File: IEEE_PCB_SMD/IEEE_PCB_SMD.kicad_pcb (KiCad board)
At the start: 2 copper layers, 98.9 x 105.3 mm, 19 parts, among them U1 555, U2 4017, U3 EG1218, U5 CR2025TR

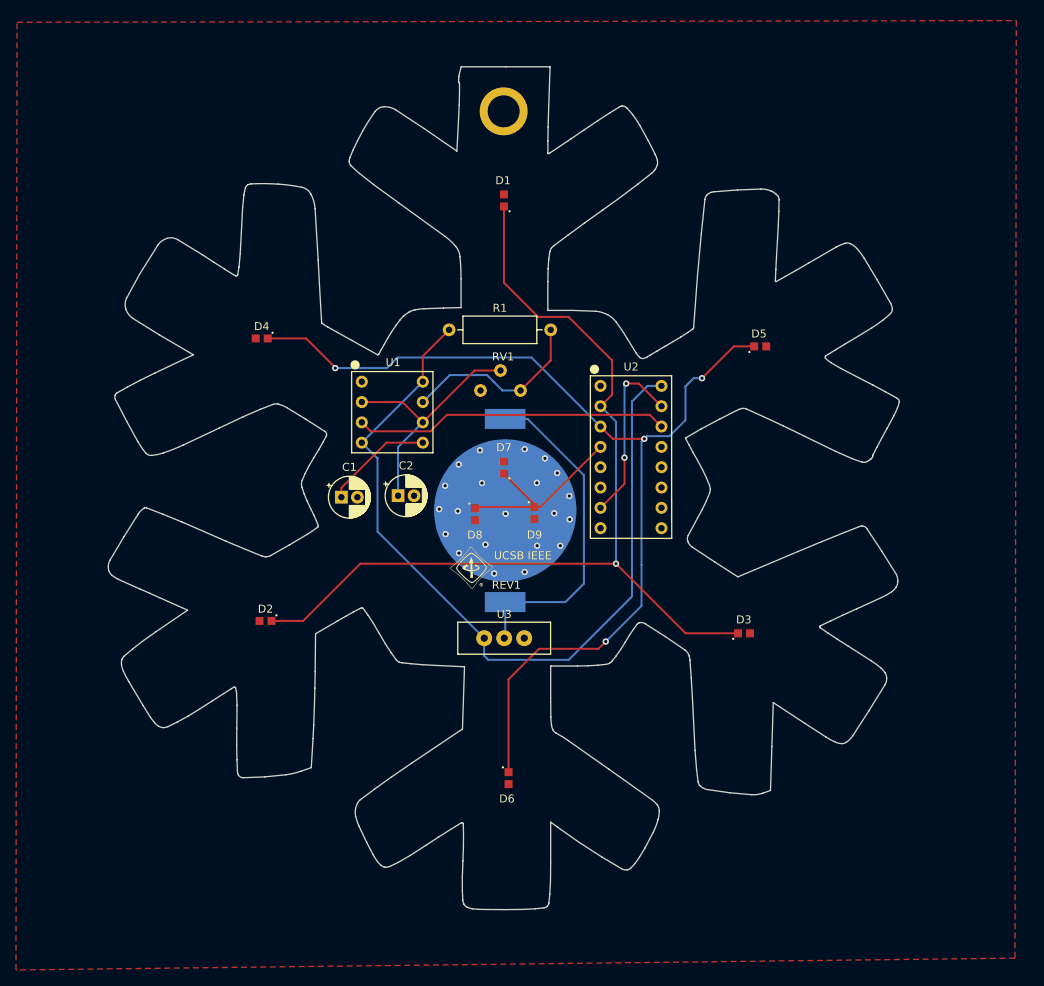
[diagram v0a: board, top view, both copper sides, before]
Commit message: Rev 10/8/22
changed the logo footprint
changed the resistor footprint
added more vias to the power
altered traces to better fit the ESR standards
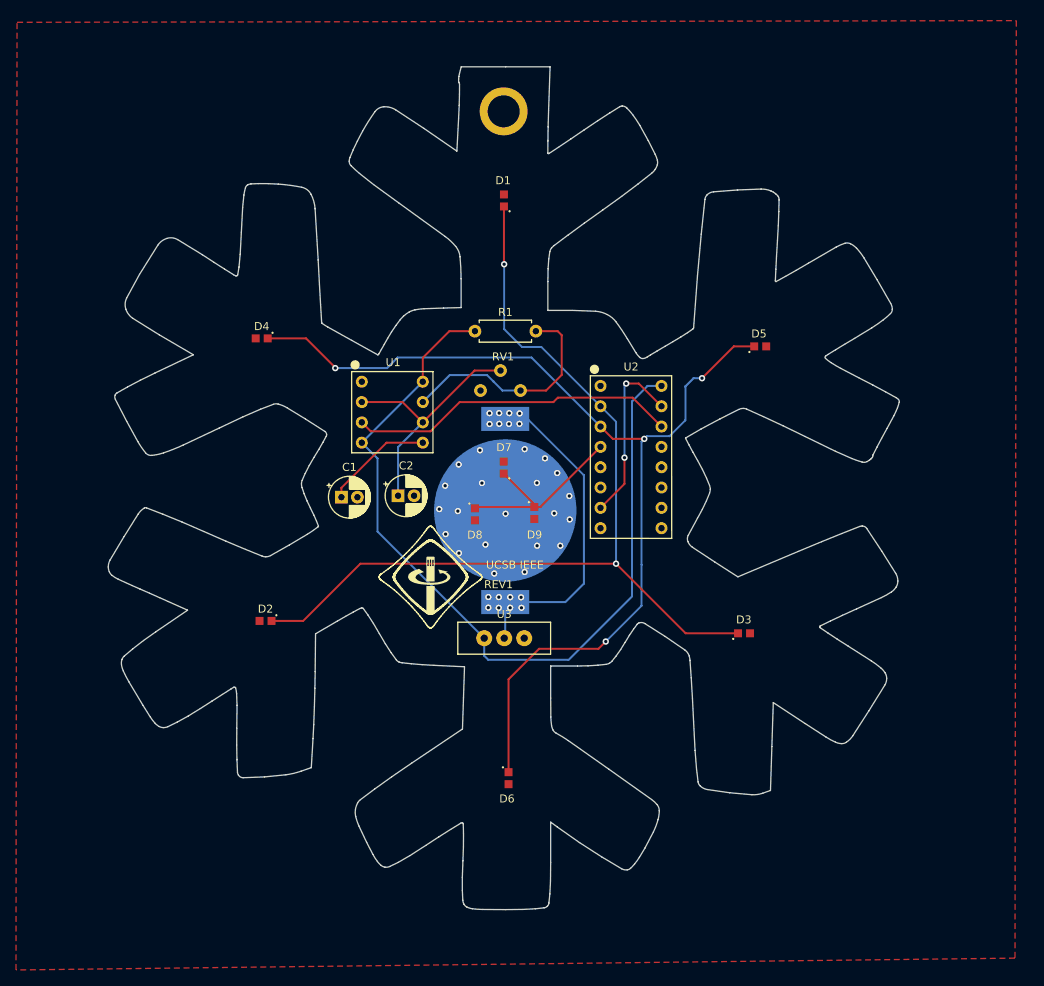
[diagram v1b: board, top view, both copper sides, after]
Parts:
- removed G***: LOGO, custom parts:IEEE Logo
- added REF**: UCSB_IEEE_Logo, custom parts:UCSB_IEEE_Logo, F.Cu at (138.8, 104.1)
- R1: footprint Resistor_THT:R_Axial_DIN0309_L9.0mm_D3.2mm_P12.70mm_Horizontal -> Resistor_THT:R_Axial_DIN0207_L6.3mm_D2.5mm_P7.62mm_Horizontal
- moved R1 3.23 mm to (144.4, 73.3)
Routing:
- net Net-(R1-Pad2): track 23.6 -> 28.8 mm
- net +3V3: track 102.4 -> 105.5 mm
- net Net-(D1-Pad2): track 118.8 -> 116.7 mm, vias 1 -> 2
- net Signal: track 39.4 -> 41.2 mm
- net Net-(U3-Pad2): vias 0 -> 16

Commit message: Rev - Matthew
Snowflake changes:
Fixed battery and switch symbols
added 100 ohm resistors 603
looked at traces - not acid traps that I see

will work on the ball soon
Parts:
- removed U3: EG1218, IEEE_Ornament:EG1218
- removed U5: CR2025TR, IEEE_Ornament:CR2025TR
- added BT1: Battery_Cell, IEEE_Ornament:CR2025TR, F.Cu at (149.5, 95.2)
- added R10: 100, Resistor_SMD:R_0603_1608Metric_Pad0.98x0.95mm_HandSolder, F.Cu at (152.4, 96.0)
- added R2: 100, Resistor_SMD:R_0603_1608Metric_Pad0.98x0.95mm_HandSolder, F.Cu at (149.5, 60.7)
- added R3: 100, Resistor_SMD:R_0603_1608Metric_Pad0.98x0.95mm_HandSolder, F.Cu at (125.9, 105.5)
- added R4: 100, Resistor_SMD:R_0603_1608Metric_Pad0.98x0.95mm_HandSolder, F.Cu at (174.6, 109.8)
- added R5: 100, Resistor_SMD:R_0603_1608Metric_Pad0.98x0.95mm_HandSolder, F.Cu at (124.2, 75.8)
- added R6: 100, Resistor_SMD:R_0603_1608Metric_Pad0.98x0.95mm_HandSolder, F.Cu at (177.7, 76.0)
- added R7: 100, Resistor_SMD:R_0603_1608Metric_Pad0.98x0.95mm_HandSolder, F.Cu at (150.0, 122.4)
- added R8: 100, Resistor_SMD:R_0603_1608Metric_Pad0.98x0.95mm_HandSolder, F.Cu at (149.5, 92.2)
- added R9: 100, Resistor_SMD:R_0603_1608Metric_Pad0.98x0.95mm_HandSolder, F.Cu at (146.8, 96.0)
- added SW1: EG1218, IEEE_Ornament:EG1218, F.Cu at (149.5, 111.5)
- moved D9 3.17 mm to (153.3, 98.9)
- moved D5 3.12 mm to (182.8, 73.7)
- moved D8 3.12 mm to (145.9, 99.0)
- moved D7 2.32 mm to (149.5, 88.7)
- moved D1 1.65 mm to (149.5, 56.2)
- moved U1 1.59 mm to (131.7, 79.1)
- moved C2 1.59 mm to (136.3, 93.3)
- moved D6 1.59 mm to (150.1, 128.6)
- moved R1 1.59 mm to (145.9, 72.8)
- moved REF** 1.59 mm to (140.3, 103.5)
- moved REF** 1.59 mm to (102.0, 98.4)
- moved RV1 1.59 mm to (149.1, 80.2)
- moved C1 1.59 mm to (129.2, 93.5)
- moved D2 1.59 mm to (119.7, 109.0)
- moved D3 1.59 mm to (179.5, 110.5)
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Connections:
- D2 pad 2: Net-(D1-Pad2) -> Net-(D2-Pad2)
- D3 pad 2: Net-(D1-Pad2) -> Net-(D3-Pad2)
- D5 pad 2: Net-(D4-Pad2) -> Net-(D5-Pad2)
- D6 pad 2: Net-(D4-Pad2) -> Net-(D6-Pad2)
- D8 pad 2: Net-(D7-Pad2) -> Net-(D8-Pad2)
- D9 pad 2: Net-(D7-Pad2) -> Net-(D9-Pad2)
- U2 pad 2: Net-(D1-Pad2) -> Net-(U2-Pad2)
- U2 pad 3: Net-(D4-Pad2) -> Net-(U2-Pad3)
- U2 pad 4: Net-(D7-Pad2) -> Net-(U2-Pad4)
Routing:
- net Net-(D4-Pad2): track 127.5 -> 4.21 mm, vias 4 -> 0
- net Net-(D1-Pad2): track 116.7 -> 2.80 mm, vias 2 -> 0
- net Net-(U2-Pad3): track 0.00 -> 110.7 mm, vias 0 -> 4
- net Net-(U2-Pad2): track 0.00 -> 99.3 mm, vias 0 -> 2
- net Net-(BT1-Pad1): track 0.00 -> 42.3 mm, vias 0 -> 16
- net Net-(U3-Pad2): track 41.7 -> 0.00 mm, vias 16 -> 0
- net Net-(U2-Pad4): track 0.00 -> 31.9 mm
- net Net-(D7-Pad2): track 24.7 -> 1.91 mm
- net Net-(D2-Pad2): track 0.00 -> 5.94 mm
- net Net-(D6-Pad2): track 0.00 -> 4.56 mm
- net Net-(D5-Pad2): track 0.00 -> 4.37 mm
- net Net-(D3-Pad2): track 0.00 -> 3.48 mm
- net Net-(D8-Pad2): track 0.00 -> 2.21 mm
- net Net-(D9-Pad2): track 0.00 -> 2.11 mm
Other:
- board size 98.9 x 105.3 mm -> 98.9 x 105.4 mm

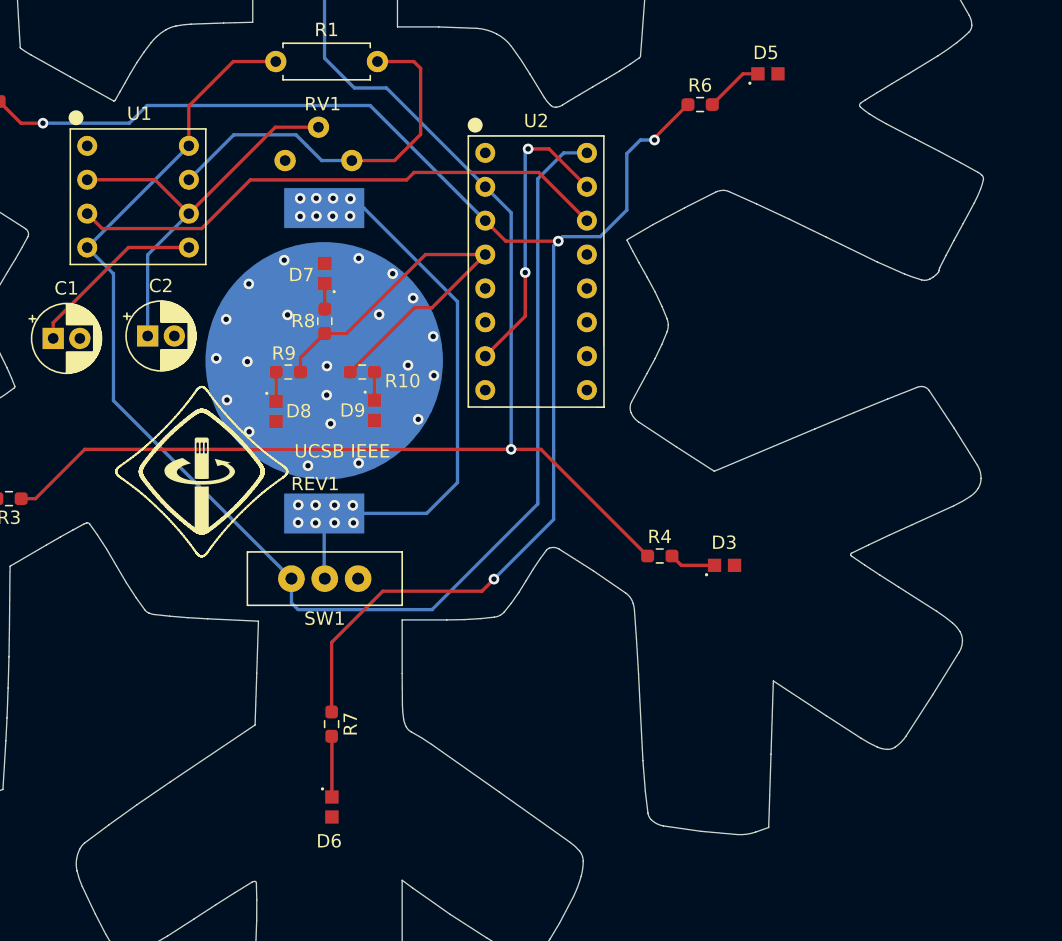
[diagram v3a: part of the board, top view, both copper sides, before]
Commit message: update schematic, pot footprint
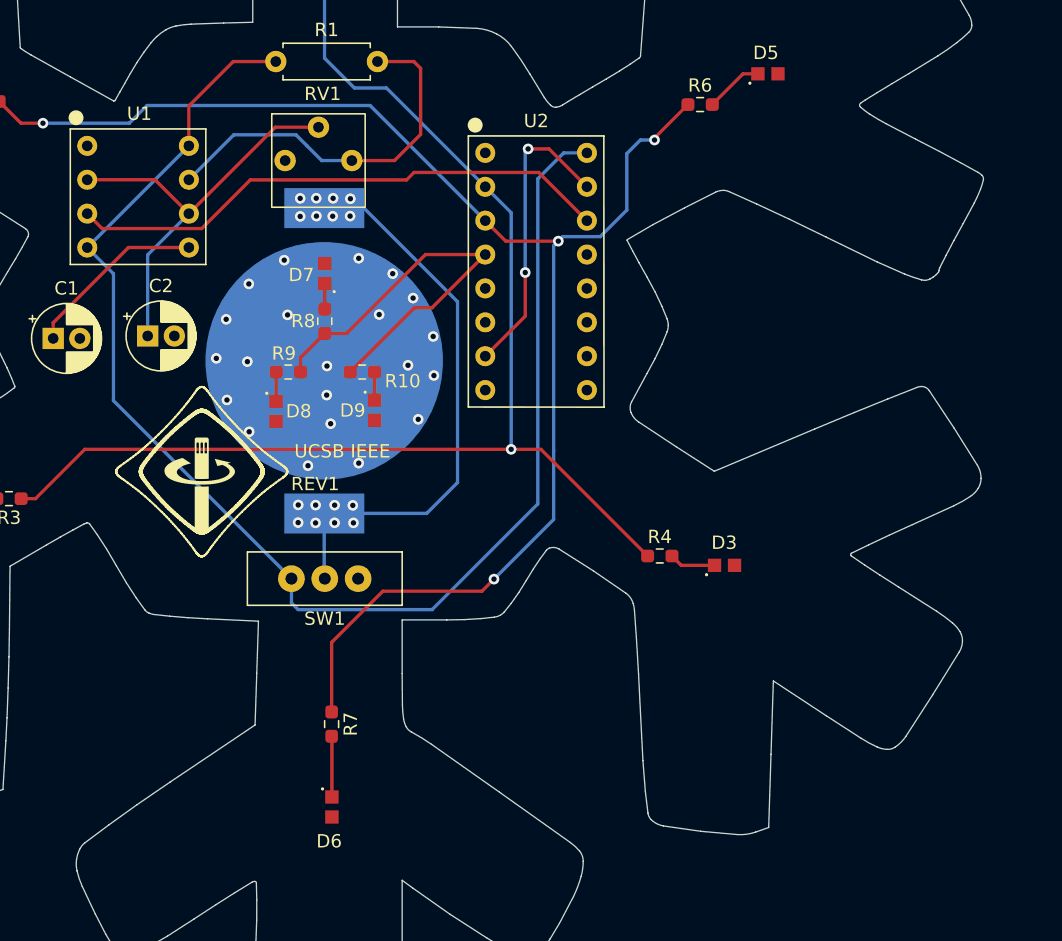
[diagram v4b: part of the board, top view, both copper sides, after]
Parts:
- RV1: footprint IEEE_Ornament:CT6EP504 -> IEEEOrnament:CT6EP504
